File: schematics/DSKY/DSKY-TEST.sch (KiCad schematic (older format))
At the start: 61 parts, among them J203 Conn_02x08, J204 Conn_02x10, J300 RPI_Connector, Q17 2N3904, Q18 2N3904, Q19 2N3904, Q20 2N3904, Q21 2N3904, Q22 2N3904, Q23 2N3904, Q24 2N3904, Q25 2N3904, Q26 2N3904, Q27 2N3904, Q28 2N3904, Q29 2N3904, Q30 2N3904, Q31 2N3904, Q32 2N3904, Q33 2N3904, Q34 2N3904, Q35 2N3904, U80 74HC245

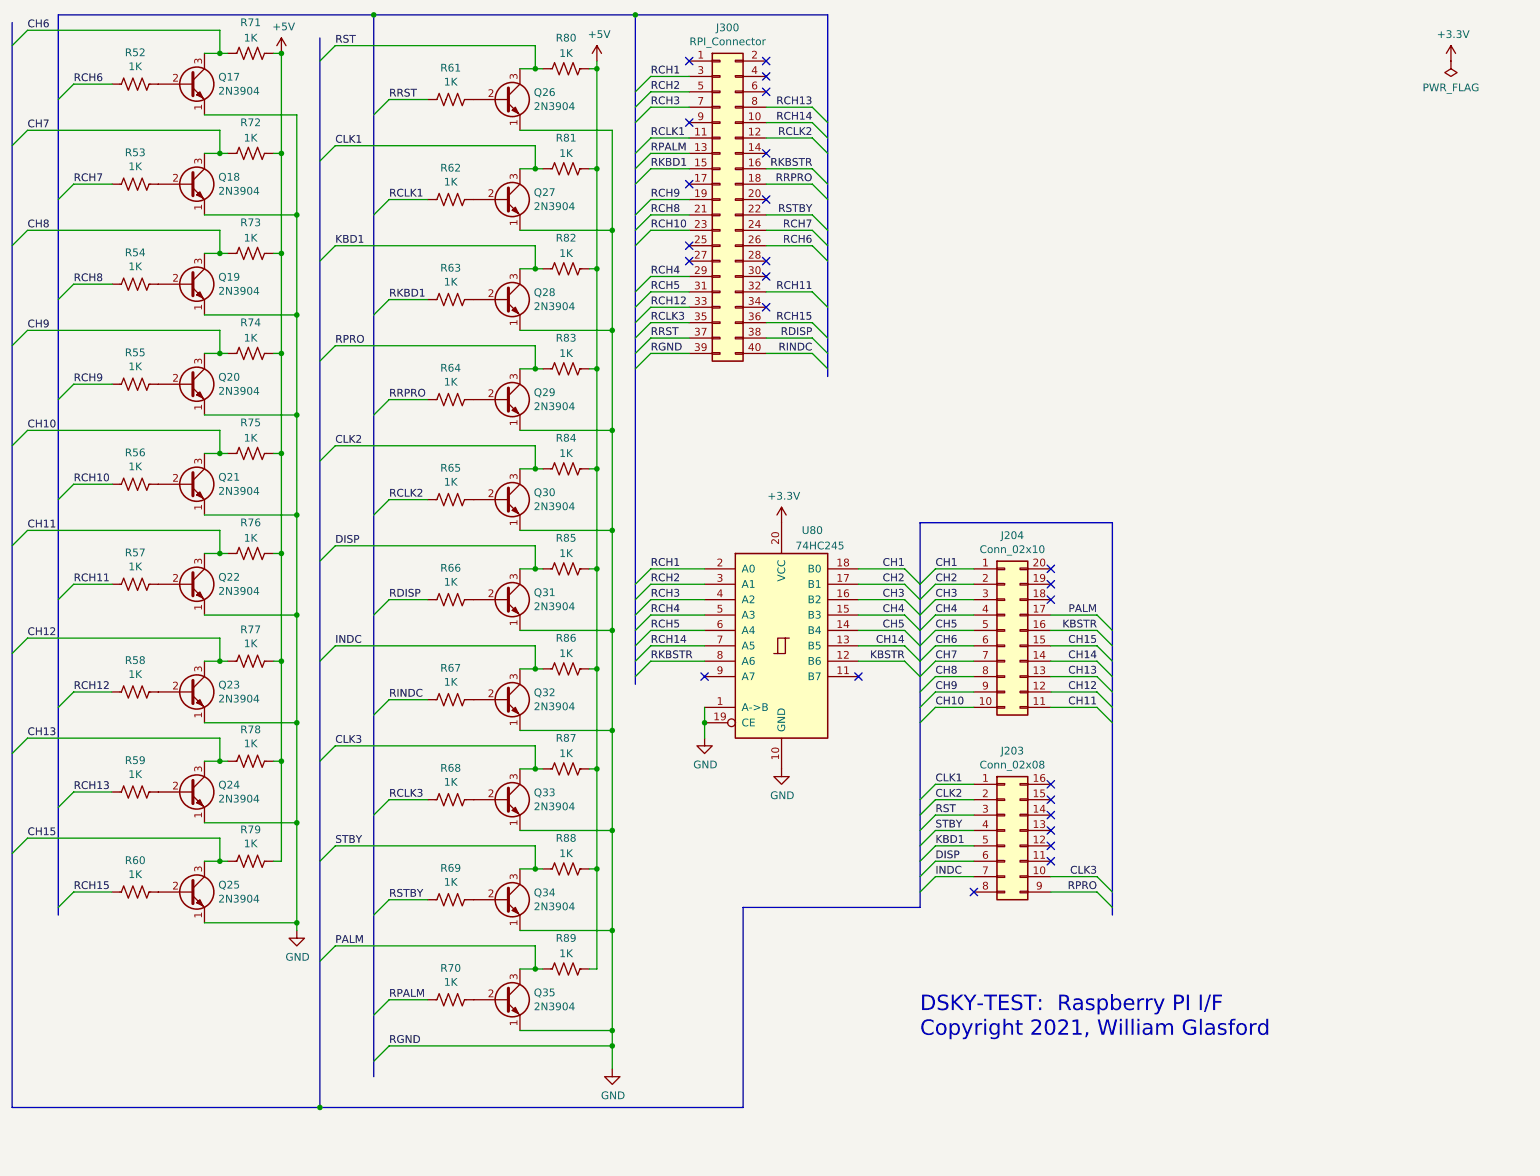
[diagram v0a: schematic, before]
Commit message: Using 4 LED driver chips.
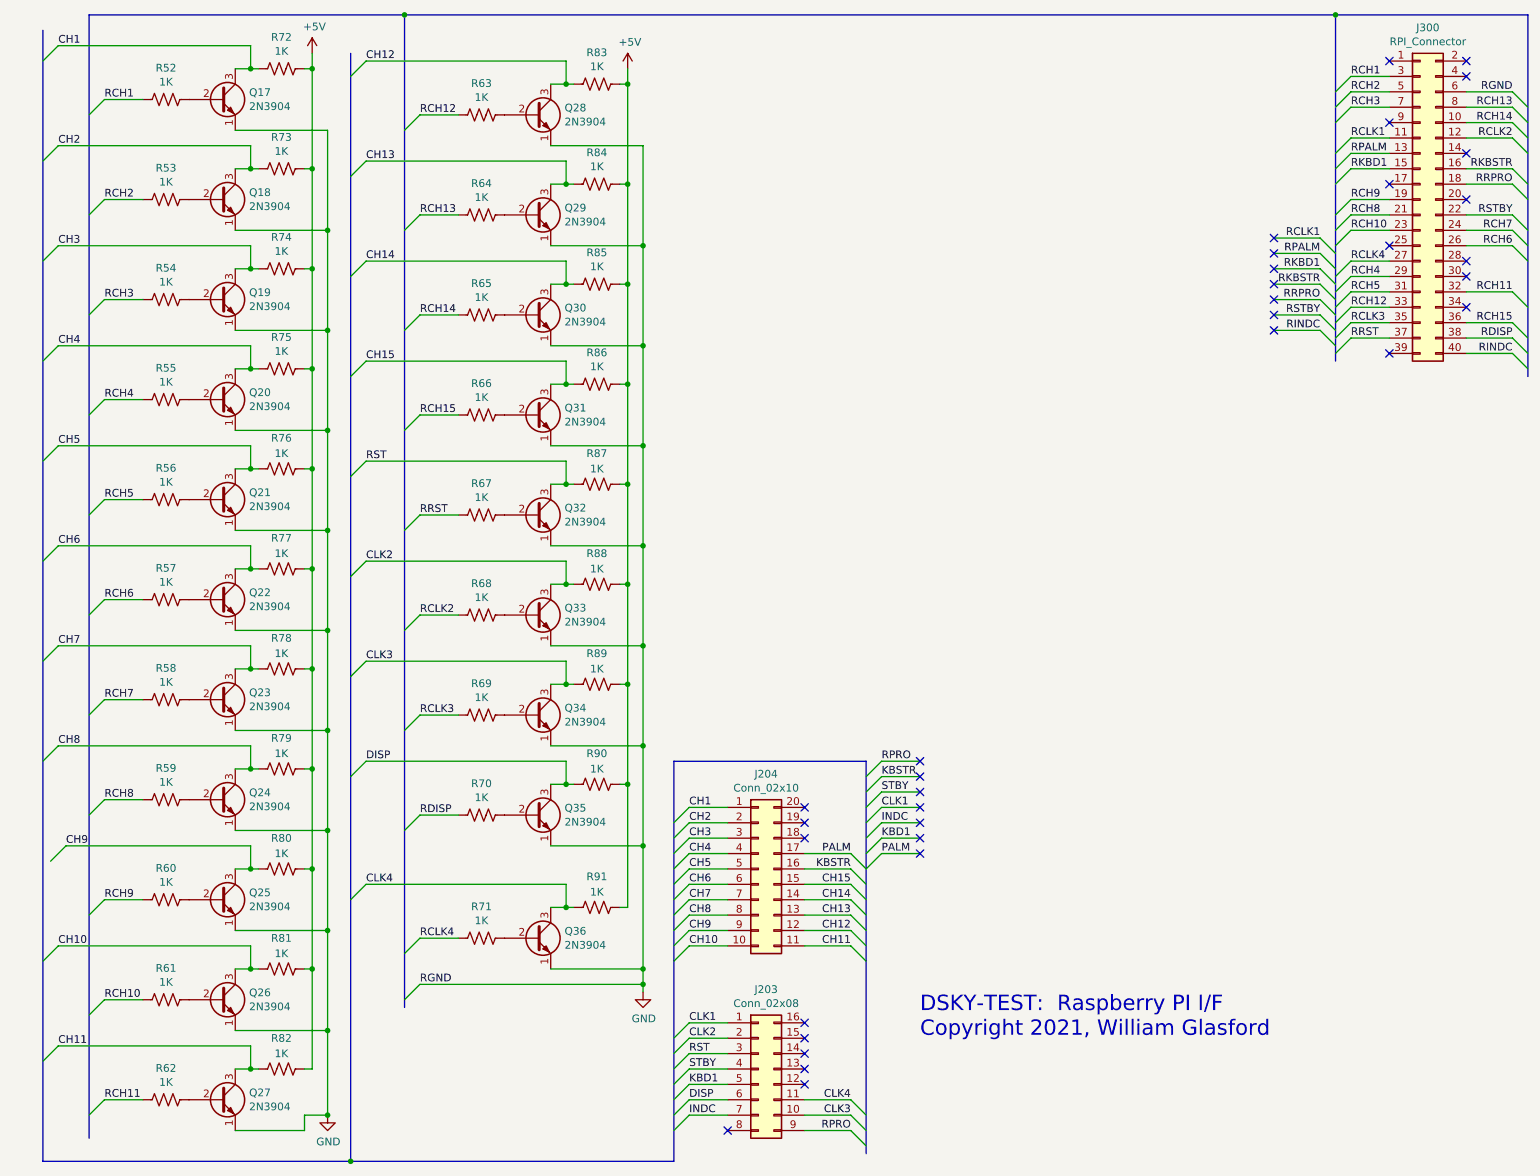
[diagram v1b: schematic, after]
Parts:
- removed U80: 74HC245, symbol 74xx:74HC245
- added Q36: 2N3904, Package_TO_SOT_THT:TO-92_Inline, symbol Transistor_BJT:2N3904
- added R90, R91: 1K, symbol Device:R_US
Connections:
- net +5V: now also R90.1, R91.1; no longer R71.1
- net CH1: now also Q17.3 (C), R72.2
- net CH10: now also Q26.3 (C), R81.2; no longer Q21.3 (C), R75.2
- net CH11: now also Q27.3 (C), R82.2; no longer Q22.3 (C), R76.2
- net CH12: now also Q28.3 (C), R83.2; no longer Q23.3 (C), R77.2
- net CH13: now also Q29.3 (C), R84.2; no longer Q24.3 (C), R78.2
- net CH14: now also Q30.3 (C), R85.2
- net CH15: now also Q31.3 (C), R86.2; no longer Q25.3 (C), R79.2
- net CH2: now also Q18.3 (C), R73.2
- net CH3: now also Q19.3 (C), R74.2
- net CH4: now also Q20.3 (C), R75.2
- net CH5: now also Q21.3 (C), R76.2
- net CH6: now also Q22.3 (C), R77.2; no longer Q17.3 (C), R71.2
- net CH7: now also Q23.3 (C), R78.2; no longer Q18.3 (C), R72.2
- net CH8: now also Q24.3 (C), R79.2; no longer Q19.3 (C), R73.2
- net CH9: now also Q25.3 (C), R80.2; no longer Q20.3 (C), R74.2
- net CLK1: no longer Q27.3 (C), R81.2
- net CLK2: now also Q33.3 (C), R88.2; no longer Q30.3 (C), R84.2
- net CLK3: now also Q34.3 (C), R89.2; no longer Q33.3 (C), R87.2
- net DISP: now also Q35.3 (C), R90.2; no longer Q31.3 (C), R85.2
- net GND: now also J300.6 (Pin_6), Q36.1 (E); no longer J300.39 (Pin_39)
- net INDC: no longer Q32.3 (C), R86.2
- net KBD1: no longer Q28.3 (C), R82.2
- net PALM: no longer Q35.3 (C), R89.2
- net RCH1: now also R52.2
- net RCH10: now also R61.2; no longer R56.2
- net RCH11: now also R62.2; no longer R57.2
- net RCH12: now also R63.2; no longer R58.2
- net RCH13: now also R64.2; no longer R59.2
- net RCH14: now also R65.2
- net RCH15: now also R66.2; no longer R60.2
- net RCH2: now also R53.2
- net RCH3: now also R54.2
- net RCH4: now also R55.2
- net RCH5: now also R56.2
- net RCH6: now also R57.2; no longer R52.2
- net RCH7: now also R58.2; no longer R53.2
- net RCH8: now also R59.2; no longer R54.2
- net RCH9: now also R60.2; no longer R55.2
- net RCLK1: no longer R62.2
- net RCLK2: now also R68.2; no longer R65.2
- net RCLK3: now also R69.2; no longer R68.2
- net RDISP: now also R70.2; no longer R66.2
- net RINDC: no longer R67.2
- net RKBD1: no longer R63.2
- net RPALM: no longer R70.2
- net RPRO: no longer Q29.3 (C), R83.2
- net RRPRO: no longer R64.2
- net RRST: now also R67.2; no longer R61.2
- net RST: now also Q32.3 (C), R87.2; no longer Q26.3 (C), R80.2
- net RSTBY: no longer R69.2
- net STBY: no longer Q34.3 (C), R88.2
- net CLK4: now reaches J203.11 (Pin_11)
- net CLK4: now also Q36.3 (C), R91.2
- net RCLK4: now reaches J300.27 (Pin_27)
- net RCLK4: now also R71.2
- new net: Q36.2 (B), R71.1
- no-connect marks 25 -> 35

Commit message: Modified to use fourth display decoder chip.
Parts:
- removed Q17, Q18, Q19, Q20, Q21, Q22, Q23, Q24, Q25, Q26, Q27, Q28, Q29, Q30, Q31, Q32, Q33, Q34, Q35, Q36: 2N3904, Package_TO_SOT_THT:TO-92_Inline, symbol Transistor_BJT:2N3904
- removed R52, R53, R54, R55, R56, R57, R58, R59, R60, R61, R62, R63, R64, R65, R66, R67, R68, R69, R70, R71, R72, R73, R74, R75, R76, R77, R78, R79, R80, R81, R82, R83, R84, R85, R86, R87, R88, R89, R90, R91: 1K, symbol Device:R_US
- added U87, U88, U89, U90, U91: 74LS245, symbol 74xx:74LS245
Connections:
- net labels added: 3.3V, CHDIR
- net labels removed: CLK4, RCLK4
- wire segments 252 -> 127
- no-connect marks 35 -> 49
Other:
- moved on the sheet: J203, J204, J300
